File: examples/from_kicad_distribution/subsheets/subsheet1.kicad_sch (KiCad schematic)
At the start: 3 parts

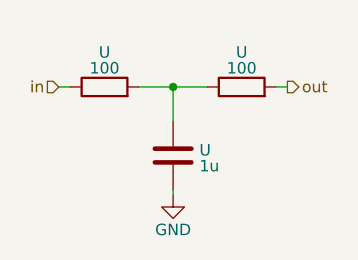
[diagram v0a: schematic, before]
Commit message: fixed subsheets. all examples now working
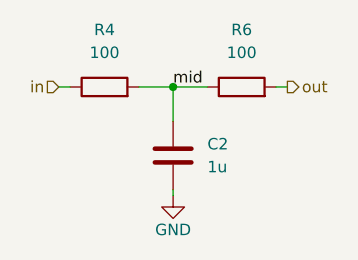
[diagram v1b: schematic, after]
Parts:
- removed U: 1u, symbol Device:C
- removed U (x2): 100, symbol Device:R
- added C2: 1u, symbol Device:C
- added R4, R6: 100, symbol Device:R
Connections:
- net GND: now also C2.2
- net in: now also R4.1
- net out: now also R6.2
- new net mid: C2.1, R4.2, R6.1
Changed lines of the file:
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@@
     (stroke (width 0) (type default))
+  )
+  (label "mid" (at 161.29 87.63 0) (fields_autoplaced)
+    (effects (font (size 1.27 1.27)) (justify left bottom))
   )
   (hierarchical_label "in" (shape input) (at 148.59 87.63 180) (fields_autoplaced)
@@
   (hierarchical_label "out" (shape output) (at 173.99 87.63 0) (fields_autoplaced)
     (effects (font (size 1.27 1.27)) (justify left))
-  )
-  (symbol (lib_id "Device:C") (at 161.29 95.25 0) (unit 1)
-    (in_bom yes) (on_board yes) (dnp no) (fields_autoplaced)
-    (property "Reference" "U" (at 164.211 94.6555 0)
-      (effects (font (size 1.27 1.27)) (justify left))
-    )
-    (property "Value" "1u" (at 164.211 96.4177 0)
-      (effects (font (size 1.27 1.27)) (justify left))
-    )
-    (property "Footprint" "" (at 162.2552 99.06 0)
-      (effects (font (size 1.27 1.27)) hide)
-    )
-    (property "Datasheet" "~" (at 161.29 95.25 0)
-      (effects (font (size 1.27 1.27)) hide)
-    )
-    (pin "1")
-    (pin "2")
-    (instances
-      (project "subsheet1"
-        (path "/653165f2-b395-46b4-92da-df4011983d82"
-          (reference "U") (unit 1)
-        )
-      )
-      (project "subsheets"
-        (path "/e63e39d7-6ac0-4ffd-8aa3-1841a4541b55/51ab3a6c-36b1-4056-a2d2-39c83ee99c02"
-          (reference "C2") (unit 1)
-        )
-      )
-    )
   )
   (symbol (lib_id "power:GND") (at 161.29 99.695 0) (unit 1)
@@
   (symbol (lib_id "Device:R") (at 168.91 87.63 90) (unit 1)
     (in_bom yes) (on_board yes) (dnp no) (fields_autoplaced)
-    (property "Reference" "U" (at 168.91 83.7819 90)
+    (property "Reference" "R6" (at 168.91 81.28 90)
       (effects (font (size 1.27 1.27)))
     )
-    (property "Value" "100" (at 168.91 85.5441 90)
+    (property "Value" "100" (at 168.91 83.82 90)
       (effects (font (size 1.27 1.27)))
     )
@@
     (pin "2")
     (instances
-      (project "subsheet1"
-        (path "/653165f2-b395-46b4-92da-df4011983d82"
-          (reference "U") (unit 1)
-        )
-      )
       (project "subsheets"
         (path "/e63e39d7-6ac0-4ffd-8aa3-1841a4541b55/51ab3a6c-36b1-4056-a2d2-39c83ee99c02"
@@
     )
   )
+  (symbol (lib_id "Device:C") (at 161.29 95.25 0) (unit 1)
+    (in_bom yes) (on_board yes) (dnp no) (fields_autoplaced)
+    (property "Reference" "C2" (at 165.1 93.98 0)
+      (effects (font (size 1.27 1.27)) (justify left))
+    )
+    (property "Value" "1u" (at 165.1 96.52 0)
+      (effects (font (size 1.27 1.27)) (justify left))
+    )
+    (property "Footprint" "" (at 162.2552 99.06 0)
+      (effects (font (size 1.27 1.27)) hide)
+    )
+    (property "Datasheet" "~" (at 161.29 95.25 0)
+      (effects (font (size 1.27 1.27)) hide)
+    )
+    (pin "2")
+    (pin "1")
+    (instances
+      (project "subsheets"
+        (path "/e63e39d7-6ac0-4ffd-8aa3-1841a4541b55/51ab3a6c-36b1-4056-a2d2-39c83ee99c02"
+          (reference "C2") (unit 1)
+        )
+      )
+    )
+  )
   (symbol (lib_id "Device:R") (at 153.67 87.63 90) (unit 1)
     (in_bom yes) (on_board yes) (dnp no) (fields_autoplaced)
-    (property "Reference" "U" (at 153.67 83.7819 90)
+    (property "Reference" "R4" (at 153.67 81.28 90)
       (effects (font (size 1.27 1.27)))
     )
-    (property "Value" "100" (at 153.67 85.5441 90)
+    (property "Value" "100" (at 153.67 83.82 90)
       (effects (font (size 1.27 1.27)))
     )
@@
     (pin "2")
     (instances
-      (project "subsheet1"
-        (path "/653165f2-b395-46b4-92da-df4011983d82"
-          (reference "U") (unit 1)
-        )
-      )
       (project "subsheets"
         (path "/e63e39d7-6ac0-4ffd-8aa3-1841a4541b55/51ab3a6c-36b1-4056-a2d2-39c83ee99c02"
